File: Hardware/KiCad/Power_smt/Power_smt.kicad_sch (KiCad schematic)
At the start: 10 parts, among them IC1 LM2596TV, J1 JACK-PLUG0

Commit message: power board kicad smt
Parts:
- C1: MPN (none) -> CC0402MRX5R5BB106
- C2, C4: MPN (none) -> CC0603MRX5R5BB226
- C3: MPN (none) -> CC0402KRX7R7BB104
- GND0, UNK5V0: MPN (none) -> DNI
- IC1: MPN (none) -> AP63205WU-7
- JP1: footprint switched-lm2575:1X02 -> Connector_PinHeader_2.54mm:PinHeader_1x02_P2.54mm_Vertical_SMD_Pin1Right; MPN (none) -> TSM-102-01-L-SV-TR
- L1: footprint (none) -> Inductor_SMD:L_1008_2520Metric; MPN (none) -> CIGW252010GL4R7MNE
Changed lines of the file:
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@@
       (effects (font (size 1.27 1.27)) hide)
     )
-    (property "MPN" "" (at 195.58 101.6 0)
+    (property "MPN" "CC0603MRX5R5BB226" (at 195.58 101.6 0)
       (effects (font (size 1.27 1.27)) hide)
     )
@@
   (symbol (lib_id "switched-lm2575-eagle-import:GND") (at 152.4 106.68 0) (unit 1)
     (in_bom yes) (on_board yes) (dnp no)
-    (property "Reference" "#GND3" (at 152.4 106.68 0)
+    (property "Reference" "#GND03" (at 152.4 106.68 0)
       (effects (font (size 1.27 1.27)) hide)
     )
@@
       (project "Power_smt"
         (path "/f755320a-8d72-40d8-8615-96171d840dc8"
-          (reference "#GND3") (unit 1)
+          (reference "#GND03") (unit 1)
         )
       )
@@
       (effects (font (size 1.27 1.27)) hide)
     )
-    (property "MPN" "" (at 104.14 116.84 0)
+    (property "MPN" "DNI" (at 104.14 116.84 0)
       (effects (font (size 1.27 1.27)) hide)
     )
@@
   (symbol (lib_id "switched-lm2575-eagle-import:GND") (at 201.93 107.95 0) (unit 1)
     (in_bom yes) (on_board yes) (dnp no)
-    (property "Reference" "#GND6" (at 201.93 107.95 0)
+    (property "Reference" "#GND06" (at 201.93 107.95 0)
       (effects (font (size 1.27 1.27)) hide)
     )
@@
       (project "Power_smt"
         (path "/f755320a-8d72-40d8-8615-96171d840dc8"
-          (reference "#GND6") (unit 1)
+          (reference "#GND06") (unit 1)
         )
       )
@@
   (symbol (lib_id "switched-lm2575-eagle-import:GND") (at 106.68 121.92 0) (unit 1)
     (in_bom yes) (on_board yes) (dnp no)
-    (property "Reference" "#GND1" (at 106.68 121.92 0)
+    (property "Reference" "#GND01" (at 106.68 121.92 0)
       (effects (font (size 1.27 1.27)) hide)
     )
@@
       (project "Power_smt"
         (path "/f755320a-8d72-40d8-8615-96171d840dc8"
-          (reference "#GND1") (unit 1)
+          (reference "#GND01") (unit 1)
         )
       )
@@
   (symbol (lib_id "switched-lm2575-eagle-import:GND") (at 114.3 104.14 0) (unit 1)
     (in_bom yes) (on_board yes) (dnp no)
-    (property "Reference" "#GND4" (at 114.3 104.14 0)
+    (property "Reference" "#GND04" (at 114.3 104.14 0)
       (effects (font (size 1.27 1.27)) hide)
     )
@@
       (project "Power_smt"
         (path "/f755320a-8d72-40d8-8615-96171d840dc8"
-          (reference "#GND4") (unit 1)
+          (reference "#GND04") (unit 1)
         )
       )
@@
       (effects (font (size 1.27 1.27)) hide)
     )
-    (property "MPN" "" (at 207.01 101.6 0)
+    (property "MPN" "CC0603MRX5R5BB226" (at 207.01 101.6 0)
       (effects (font (size 1.27 1.27)) hide)
     )
@@
       (effects (font (size 1.778 1.5113)) (justify left bottom) hide)
     )
-    (property "Footprint" "switched-lm2575:1X02" (at 106.68 83.82 0)
+    (property "Footprint" "Connector_PinHeader_2.54mm:PinHeader_1x02_P2.54mm_Vertical_SMD_Pin1Right" (at 106.68 83.82 0)
       (effects (font (size 1.27 1.27)) hide)
     )
@@
       (effects (font (size 1.27 1.27)) hide)
     )
-    (property "MPN" "" (at 106.68 83.82 0)
+    (property "MPN" "TSM-102-01-L-SV-TR" (at 106.68 83.82 0)
       (effects (font (size 1.27 1.27)) hide)
     )
@@
       (effects (font (size 1.27 1.27)))
     )
-    (property "Footprint" "" (at 185.42 93.98 0)
+    (property "Footprint" "Inductor_SMD:L_1008_2520Metric" (at 185.42 93.98 0)
       (effects (font (size 1.27 1.27)) hide)
     )
@@
       (effects (font (size 1.27 1.27)) hide)
     )
-    (property "MPN" "" (at 185.42 93.98 0)
+    (property "MPN" "CIGW252010GL4R7MNE" (at 185.42 93.98 0)
       (effects (font (size 1.27 1.27)) hide)
     )
@@
       (effects (font (size 1.27 1.27)) hide)
     )
-    (property "MPN" "" (at 176.53 97.79 0)
+    (property "MPN" "CC0402KRX7R7BB104" (at 176.53 97.79 0)
       (effects (font (size 1.27 1.27)) hide)
     )
@@
   (symbol (lib_id "switched-lm2575-eagle-import:VCC") (at 215.9 88.9 0) (unit 1)
     (in_bom yes) (on_board yes) (dnp no)
-    (property "Reference" "#P+1" (at 215.9 88.9 0)
+    (property "Reference" "#P+01" (at 215.9 88.9 0)
       (effects (font (size 1.27 1.27)) hide)
     )
@@
       (project "Power_smt"
         (path "/f755320a-8d72-40d8-8615-96171d840dc8"
-          (reference "#P+1") (unit 1)
+          (reference "#P+01") (unit 1)
         )
       )
@@
       (effects (font (size 1.27 1.27)) hide)
     )
-    (property "MPN" "" (at 114.3 97.79 0)
+    (property "MPN" "CC0402MRX5R5BB106" (at 114.3 97.79 0)
       (effects (font (size 1.27 1.27)) hide)
     )
@@
       (effects (font (size 1.27 1.27)) hide)
     )
-    (property "MPN" "" (at 215.9 96.52 0)
+    (property "MPN" "DNI" (at 215.9 96.52 0)
       (effects (font (size 1.27 1.27)) hide)
     )
@@
       (effects (font (size 1.27 1.27)) hide)
     )
-    (property "MPN" "" (at 152.4 96.52 0)
-      (effects (font (size 1.27 1.27)) hide)
-    )
+    (property "MPN" "AP63205WU-7" (at 152.4 96.52 0)
+      (effects (font (size 1.27 1.27)) hide)
+    )

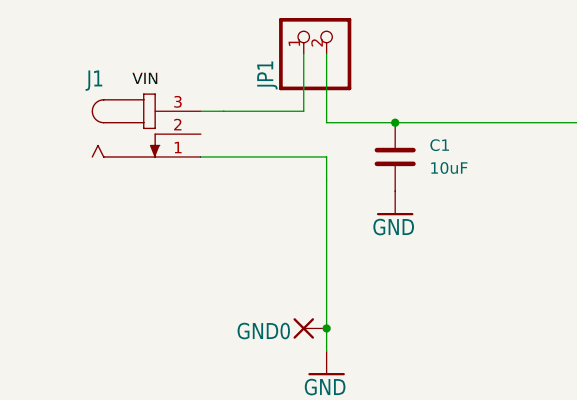
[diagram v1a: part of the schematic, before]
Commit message: SMT edits and start of fake dual ram sketching
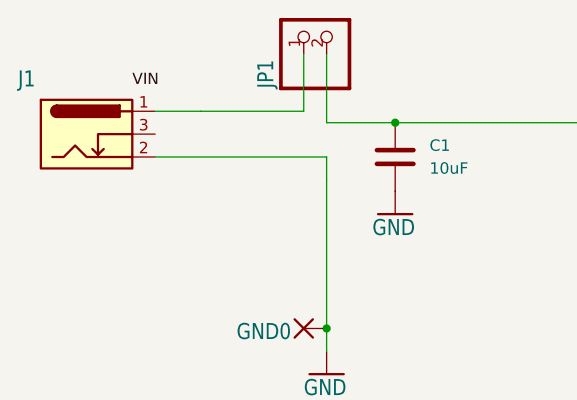
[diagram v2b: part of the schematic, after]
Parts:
- C1: MPN CC0402MRX5R5BB106 -> CC0805MRX5R5BB106
- C2, C4: MPN CC0603MRX5R5BB226 -> CC0805MRX5R5BB226
- C3: MPN CC0402KRX7R7BB104 -> CC0805KRX7R7BB104
- IC1: value LM2596TV -> AP63205WU-7
- J1: footprint Connector_BarrelJack:BarrelJack_CUI_PJ-036AH-SMT_Horizontal -> Connector_BarrelJack:BarrelJack_GCT_DCJ200-10-A_Horizontal; symbol switched-lm2575-eagle-import:JACK-PLUG0 -> Connector:Barrel_Jack_Switch; MPN PJ-036AH-SMT-TR -> DCJ200-10-A-K1-K
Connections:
- net GND: now also J1.2; no longer J1.1
- net at JP1.1: now also J1.1; no longer J1.3
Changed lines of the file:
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@@
-    (stroke (width 0) (type default))
-  )
-  (wire (pts (xy 95.25 92.71) (xy 104.14 92.71))
     (stroke (width 0) (type default))
   )
@@
     (stroke (width 0) (type default))
   )
-  (wire (pts (xy 92.71 92.71) (xy 95.25 92.71))
+  (wire (pts (xy 92.71 92.71) (xy 87.63 92.71))
     (stroke (width 0.1524) (type solid))
   )
@@
     (stroke (width 0) (type default))
   )
+  (wire (pts (xy 92.71 92.71) (xy 104.14 92.71))
+    (stroke (width 0) (type default))
+  )
   (wire (pts (xy 104.14 92.71) (xy 104.14 86.36))
     (stroke (width 0) (type default))
@@
     (stroke (width 0) (type default))
   )
-  (wire (pts (xy 92.71 97.79) (xy 106.68 97.79))
+  (wire (pts (xy 87.63 97.79) (xy 106.68 97.79))
     (stroke (width 0) (type default))
   )
@@
       (effects (font (size 1.27 1.27)) hide)
     )
-    (property "MPN" "CC0603MRX5R5BB226" (at 195.58 101.6 0)
+    (property "MPN" "CC0805MRX5R5BB226" (at 195.58 101.6 0)
       (effects (font (size 1.27 1.27)) hide)
     )
@@
       (effects (font (size 1.27 1.27)) hide)
     )
-    (property "MPN" "CC0603MRX5R5BB226" (at 207.01 101.6 0)
+    (property "MPN" "CC0805MRX5R5BB226" (at 207.01 101.6 0)
       (effects (font (size 1.27 1.27)) hide)
     )
@@
       (effects (font (size 1.27 1.27)) hide)
     )
-    (property "MPN" "CC0402KRX7R7BB104" (at 176.53 97.79 0)
+    (property "MPN" "CC0805KRX7R7BB104" (at 176.53 97.79 0)
       (effects (font (size 1.27 1.27)) hide)
     )
@@
       (effects (font (size 1.27 1.27)) hide)
     )
-    (property "MPN" "CC0402MRX5R5BB106" (at 114.3 97.79 0)
+    (property "MPN" "CC0805MRX5R5BB106" (at 114.3 97.79 0)
       (effects (font (size 1.27 1.27)) hide)
     )
@@
       (effects (font (size 1.778 1.5113)) (justify left bottom))
     )
-    (property "Value" "LM2596TV" (at 154.94 90.17 0)
+    (property "Value" "AP63205WU-7" (at 154.94 90.17 0)
       (effects (font (size 1.778 1.5113)) (justify left bottom) hide)
     )
@@
     )
   )
-  (symbol (lib_id "switched-lm2575-eagle-import:JACK-PLUG0") (at 87.63 95.25 0) (unit 1)
-    (in_bom yes) (on_board yes) (dnp no)
-    (property "Reference" "J1" (at 80.01 90.17 0)
-      (effects (font (size 1.778 1.5113)) (justify left bottom))
-    )
-    (property "Value" "JACK-PLUG0" (at 80.01 100.33 0)
+  (symbol (lib_id "Connector:Barrel_Jack_Switch") (at 80.01 95.25 0) (unit 1)
+    (in_bom yes) (on_board yes) (dnp no)
+    (property "Reference" "J1" (at 72.39 90.17 0)
+      (effects (font (size 1.778 1.5113)) (justify left bottom))
+    )
+    (property "Value" "JACK-PLUG0" (at 72.39 100.33 0)
       (effects (font (size 1.778 1.5113)) (justify left bottom) hide)
     )
-    (property "Footprint" "Connector_BarrelJack:BarrelJack_CUI_PJ-036AH-SMT_Horizontal" (at 87.63 95.25 0)
-      (effects (font (size 1.27 1.27)) hide)
-    )
-    (property "Datasheet" "" (at 87.63 95.25 0)
-      (effects (font (size 1.27 1.27)) hide)
-    )
-    (property "MPN" "PJ-036AH-SMT-TR" (at 87.63 95.25 0)
-      (effects (font (size 1.27 1.27)) hide)
-    )
+    (property "Footprint" "Connector_BarrelJack:BarrelJack_GCT_DCJ200-10-A_Horizontal" (at 81.28 96.266 0)
+      (effects (font (size 1.27 1.27)) hide)
+    )
+    (property "Datasheet" "~" (at 81.28 96.266 0)
+      (effects (font (size 1.27 1.27)) hide)
+    )
+    (property "MPN" "DCJ200-10-A-K1-K" (at 80.01 95.25 0)
+      (effects (font (size 1.27 1.27)) hide)
+    )

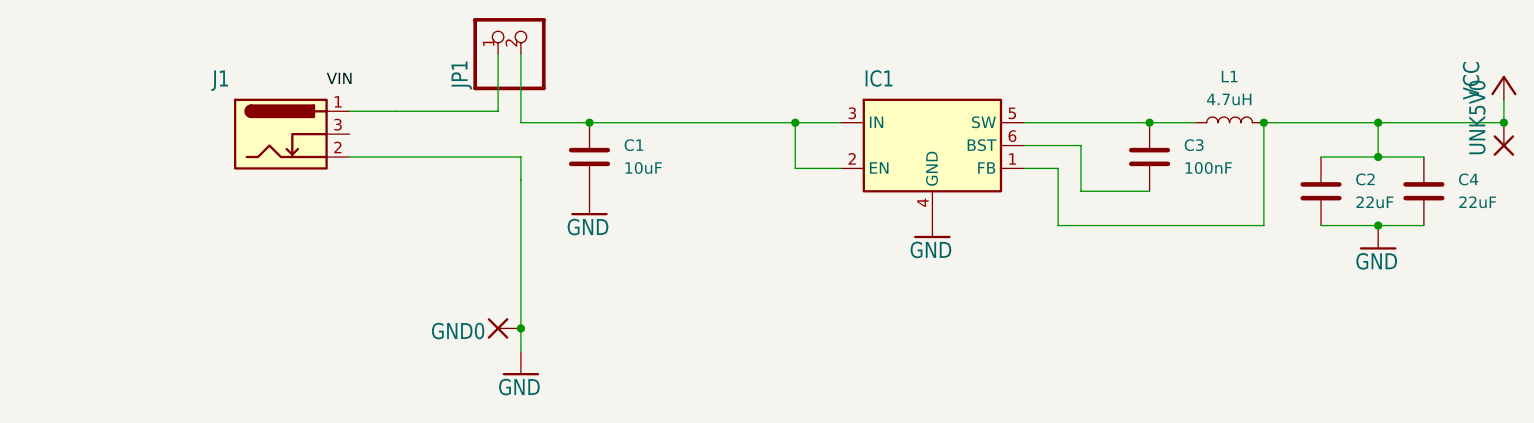
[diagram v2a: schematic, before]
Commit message: updates to kicad smt versions
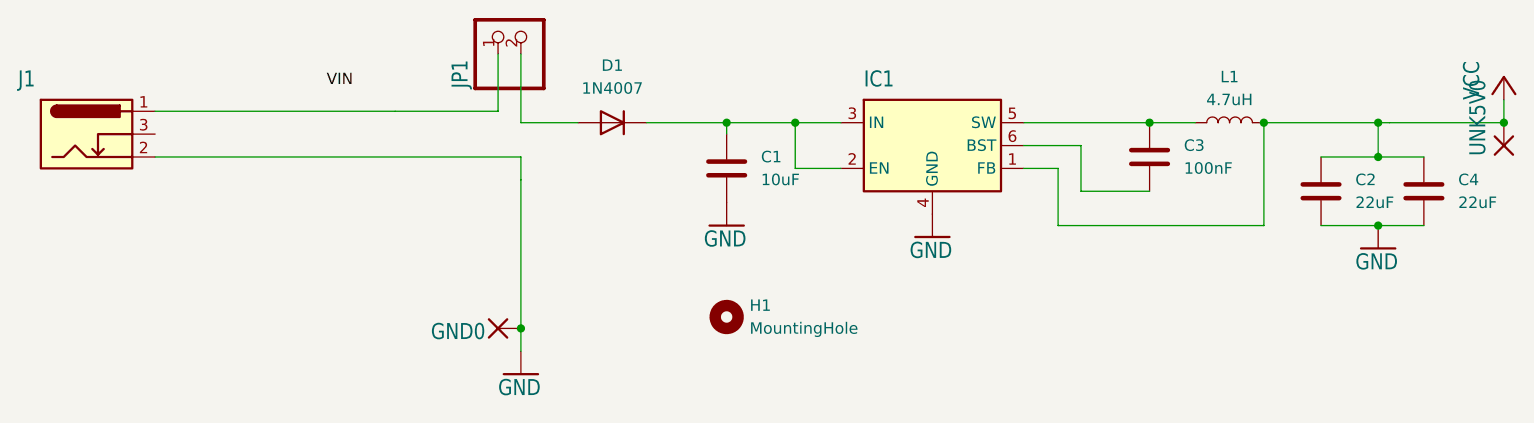
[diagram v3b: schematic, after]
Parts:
- added D1: 1N4007, Diode_SMD:D_SOD-123F, symbol Diode:1N4007
- added H1: MountingHole, MountingHole:MountingHole_3.2mm_M3, symbol Mechanical:MountingHole
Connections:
- net at C1.1, IC1.2 (EN), IC1.3 (IN): now also D1.1 (K); no longer JP1.2
- new net: D1.2 (A), JP1.2
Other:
- moved on the sheet: C1, J1
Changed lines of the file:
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@@
 (kicad_sch (version 20230121) (generator eeschema)
   (paper "A4")
-  (junction (at 114.3 93.98) (diameter 0) (color 0 0 0 0)
+  (junction (at 129.54 93.98) (diameter 0) (color 0 0 0 0)
   )
   (junction (at 201.93 97.79) (diameter 0) (color 0 0 0 0)
@@
   (junction (at 201.93 93.98) (diameter 0) (color 0 0 0 0)
   )
+  (wire (pts (xy 129.54 93.98) (xy 137.16 93.98))
+    (stroke (width 0.1524) (type solid))
+  )
   (wire (pts (xy 201.93 97.79) (xy 207.01 97.79))
     (stroke (width 0) (type default))
@@
     (stroke (width 0) (type default))
   )
-  (wire (pts (xy 92.71 92.71) (xy 87.63 92.71))
+  (wire (pts (xy 92.71 92.71) (xy 66.04 92.71))
     (stroke (width 0.1524) (type solid))
   )
@@
     (stroke (width 0) (type default))
   )
+  (wire (pts (xy 129.54 95.25) (xy 129.54 93.98))
+    (stroke (width 0) (type default))
+  )
   (wire (pts (xy 215.9 93.98) (xy 215.9 91.44))
     (stroke (width 0.1524) (type solid))
@@
     (stroke (width 0) (type default))
   )
+  (wire (pts (xy 120.65 93.98) (xy 129.54 93.98))
+    (stroke (width 0) (type default))
+  )
   (wire (pts (xy 162.56 99.06) (xy 166.37 99.06))
     (stroke (width 0) (type default))
   )
+  (wire (pts (xy 106.68 93.98) (xy 113.03 93.98))
+    (stroke (width 0) (type default))
+  )
   (wire (pts (xy 92.71 92.71) (xy 104.14 92.71))
     (stroke (width 0) (type default))
@@
     (stroke (width 0) (type default))
   )
-  (wire (pts (xy 114.3 93.98) (xy 137.16 93.98))
-    (stroke (width 0.1524) (type solid))
-  )
   (wire (pts (xy 166.37 99.06) (xy 166.37 105.41))
     (stroke (width 0) (type default))
@@
     (stroke (width 0) (type default))
   )
-  (wire (pts (xy 87.63 97.79) (xy 106.68 97.79))
-    (stroke (width 0) (type default))
-  )
-  (wire (pts (xy 106.68 93.98) (xy 114.3 93.98))
+  (wire (pts (xy 66.04 97.79) (xy 106.68 97.79))
     (stroke (width 0) (type default))
   )
@@
     (effects (font (size 1.2446 1.2446)) (justify left bottom))
   )
+  (symbol (lib_id "Diode:1N4007") (at 116.84 93.98 180) (unit 1)
+    (in_bom yes) (on_board yes) (dnp no) (fields_autoplaced)
+    (property "Reference" "D1" (at 116.84 87.63 0)
+      (effects (font (size 1.27 1.27)))
+    )
+    (property "Value" "1N4007" (at 116.84 90.17 0)
+      (effects (font (size 1.27 1.27)))
+    )
+    (property "Footprint" "Diode_SMD:D_SOD-123F" (at 116.84 89.535 0)
+      (effects (font (size 1.27 1.27)) hide)
+    )
+    (property "Datasheet" "http://www.vishay.com/docs/88503/1n4001.pdf" (at 116.84 93.98 0)
+      (effects (font (size 1.27 1.27)) hide)
+    )
+    (property "Sim.Device" "D" (at 116.84 93.98 0)
+      (effects (font (size 1.27 1.27)) hide)
+    )
+    (property "Sim.Pins" "1=K 2=A" (at 116.84 93.98 0)
+      (effects (font (size 1.27 1.27)) hide)
+    )
+    (property "MPN" "FR1M-LTP" (at 116.84 93.98 0)
+      (effects (font (size 1.27 1.27)) hide)
+    )
+    (pin "1")
+    (pin "2")
+    (instances
+      (project "Power_smt"
+        (path "/f755320a-8d72-40d8-8615-96171d840dc8"
+          (reference "D1") (unit 1)
+        )
+      )
+    )
+  )
   (symbol (lib_id "Device:C") (at 195.58 101.6 0) (unit 1)
     (in_bom yes) (on_board yes) (dnp no) (fields_autoplaced)
@@
     )
   )
-  (symbol (lib_id "switched-lm2575-eagle-import:GND") (at 114.3 104.14 0) (unit 1)
-    (in_bom yes) (on_board yes) (dnp no)
-    (property "Reference" "#GND04" (at 114.3 104.14 0)
-      (effects (font (size 1.27 1.27)) hide)
-    )
-    (property "Value" "GND" (at 111.76 106.68 0)
-      (effects (font (size 1.778 1.5113)) (justify left bottom))
-    )
-    (property "Footprint" "" (at 114.3 104.14 0)
-      (effects (font (size 1.27 1.27)) hide)
-    )
-    (property "Datasheet" "" (at 114.3 104.14 0)
+  (symbol (lib_id "switched-lm2575-eagle-import:GND") (at 129.54 105.41 0) (unit 1)
+    (in_bom yes) (on_board yes) (dnp no)
+    (property "Reference" "#GND04" (at 129.54 105.41 0)
+      (effects (font (size 1.27 1.27)) hide)
+    )
+    (property "Value" "GND" (at 127 107.95 0)
+      (effects (font (size 1.778 1.5113)) (justify left bottom))
+    )
+    (property "Footprint" "" (at 129.54 105.41 0)
+      (effects (font (size 1.27 1.27)) hide)
+    )
+    (property "Datasheet" "" (at 129.54 105.41 0)
       (effects (font (size 1.27 1.27)) hide)
     )
@@
     )
   )
-  (symbol (lib_id "Device:C") (at 114.3 97.79 0) (unit 1)
-    (in_bom yes) (on_board yes) (dnp no) (fields_autoplaced)
-    (property "Reference" "C1" (at 118.11 96.52 0)
-      (effects (font (size 1.27 1.27)) (justify left))
-    )
-    (property "Value" "10uF" (at 118.11 99.06 0)
-      (effects (font (size 1.27 1.27)) (justify left))
-    )
-    (property "Footprint" "Capacitor_SMD:C_0805_2012Metric" (at 115.2652 101.6 0)
-      (effects (font (size 1.27 1.27)) hide)
-    )
-    (property "Datasheet" "~" (at 114.3 97.79 0)
-      (effects (font (size 1.27 1.27)) hide)
-    )
-    (property "MPN" "CC0805MRX5R5BB106" (at 114.3 97.79 0)
+  (symbol (lib_id "Device:C") (at 129.54 99.06 0) (unit 1)
+    (in_bom yes) (on_board yes) (dnp no) (fields_autoplaced)
+    (property "Reference" "C1" (at 133.35 97.79 0)
+      (effects (font (size 1.27 1.27)) (justify left))
+    )
+    (property "Value" "10uF" (at 133.35 100.33 0)
+      (effects (font (size 1.27 1.27)) (justify left))
+    )
+    (property "Footprint" "Capacitor_SMD:C_0805_2012Metric" (at 130.5052 102.87 0)
+      (effects (font (size 1.27 1.27)) hide)
+    )
+    (property "Datasheet" "~" (at 129.54 99.06 0)
+      (effects (font (size 1.27 1.27)) hide)
+    )
+    (property "MPN" "CC0805MRX5R5BB106" (at 129.54 99.06 0)
       (effects (font (size 1.27 1.27)) hide)
     )
@@
         (path "/f755320a-8d72-40d8-8615-96171d840dc8"
           (reference "UNK5V0") (unit 1)
+        )
+      )
+    )
+  )
+  (symbol (lib_id "Mechanical:MountingHole") (at 129.54 115.57 0) (unit 1)
+    (in_bom yes) (on_board yes) (dnp no) (fields_autoplaced)
+    (property "Reference" "H1" (at 132.08 114.3 0)
+      (effects (font (size 1.27 1.27)) (justify left))
+    )
+    (property "Value" "MountingHole" (at 132.08 116.84 0)
+      (effects (font (size 1.27 1.27)) (justify left))
+    )
+    (property "Footprint" "MountingHole:MountingHole_3.2mm_M3" (at 129.54 115.57 0)
+      (effects (font (size 1.27 1.27)) hide)
+    )
+    (property "Datasheet" "~" (at 129.54 115.57 0)
+      (effects (font (size 1.27 1.27)) hide)
+    )
+    (property "MPN" "DNI" (at 129.54 115.57 0)
+      (effects (font (size 1.27 1.27)) hide)
+    )
+    (instances
+      (project "Power_smt"
+        (path "/f755320a-8d72-40d8-8615-96171d840dc8"
+          (reference "H1") (unit 1)
         )
       )
@@
     )
   )
-  (symbol (lib_id "Connector:Barrel_Jack_Switch") (at 80.01 95.25 0) (unit 1)
-    (in_bom yes) (on_board yes) (dnp no)
-    (property "Reference" "J1" (at 72.39 90.17 0)
-      (effects (font (size 1.778 1.5113)) (justify left bottom))
-    )
-    (property "Value" "JACK-PLUG0" (at 72.39 100.33 0)
+  (symbol (lib_id "Connector:Barrel_Jack_Switch") (at 58.42 95.25 0) (unit 1)
+    (in_bom yes) (on_board yes) (dnp no)
+    (property "Reference" "J1" (at 50.8 90.17 0)
+      (effects (font (size 1.778 1.5113)) (justify left bottom))
+    )
+    (property "Value" "JACK-PLUG0" (at 50.8 100.33 0)
       (effects (font (size 1.778 1.5113)) (justify left bottom) hide)
     )
-    (property "Footprint" "Connector_BarrelJack:BarrelJack_GCT_DCJ200-10-A_Horizontal" (at 81.28 96.266 0)
-      (effects (font (size 1.27 1.27)) hide)
-    )
-    (property "Datasheet" "~" (at 81.28 96.266 0)
-      (effects (font (size 1.27 1.27)) hide)
-    )
-    (property "MPN" "DCJ200-10-A-K1-K" (at 80.01 95.25 0)
-      (effects (font (size 1.27 1.27)) hide)
-    )
+    (property "Footprint" "Connector_BarrelJack:BarrelJack_GCT_DCJ200-10-A_Horizontal" (at 59.69 96.266 0)
+      (effects (font (size 1.27 1.27)) hide)
+    )
+    (property "Datasheet" "~" (at 59.69 96.266 0)
+      (effects (font (size 1.27 1.27)) hide)
+    )
+    (property "MPN" "DCJ200-10-A-K1-K" (at 58.42 95.25 0)
+      (effects (font (size 1.27 1.27)) hide)
+    )
